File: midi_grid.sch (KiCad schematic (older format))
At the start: 3 parts, among them J1 USB_OTG, J2 3.5mm jack, J3 3.5mm jack

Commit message: multiple schematic and pcb changes
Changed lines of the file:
@@
 F0 "grid" 60
 F1 "grid.sch" 60
-F2 "BUTTON[1..4]" O R 4800 3400 60
-F3 "RED[1..4]" I R 4800 3000 60
-F4 "GREEN[1..4]" I R 4800 3100 60
-F5 "BLUE[1..4]" I R 4800 3200 60
+F2 "GRID_BUTTON[1..4]" O R 4800 3400 60
+F3 "PWM_RED[1..4]" I R 4800 3000 60
+F4 "PWM_GREEN[1..4]" I R 4800 3100 60
+F5 "PWM_BLUE[1..4]" I R 4800 3200 60
 F6 "COLUMN[1..6]" I R 4800 3600 60
 $EndSheet

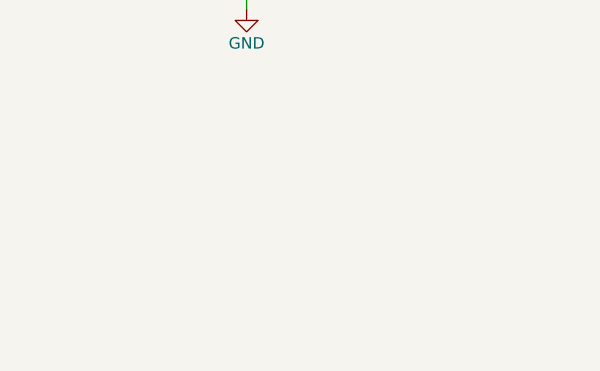
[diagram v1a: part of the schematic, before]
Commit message: added logos to pcb
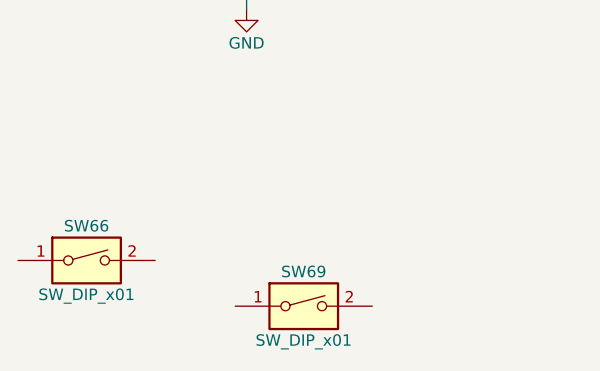
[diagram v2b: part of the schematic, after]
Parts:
- added SW66: SW_DIP_x01, ProjectLib:Logo_OSHW, symbol SW_DIP_x01
- added SW69: SW_DIP_x01, ProjectLib:qr_url, symbol SW_DIP_x01
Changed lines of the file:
@@
 NoConn ~ 2900 4600
 NoConn ~ 2900 4300
+$Comp
+L SW_DIP_x01 SW66
+U 1 1 5A53D346
+P 1800 6500
+F 0 "SW66" H 1800 6650 50  0000 C CNN
+F 1 "SW_DIP_x01" H 1800 6350 50  0000 C CNN
+F 2 "ProjectLib:Logo_OSHW" H 1800 6500 50  0001 C CNN
+F 3 "" H 1800 6500 50  0001 C CNN
+	1    1800 6500
+	1    0    0    -1
+$EndComp
+$Comp
+L SW_DIP_x01 SW69
+U 1 1 5A53DA73
+P 2750 6700
+F 0 "SW69" H 2750 6850 50  0000 C CNN
+F 1 "SW_DIP_x01" H 2750 6550 50  0000 C CNN
+F 2 "ProjectLib:qr_url" H 2750 6700 50  0001 C CNN
+F 3 "" H 2750 6700 50  0001 C CNN
+	1    2750 6700
+	1    0    0    -1
+$EndComp
 $EndSCHEMATC

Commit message: pcb development
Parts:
- GR1: renamed from SW66; value SW_DIP_x01 -> OSHW logo; symbol SW_DIP_x01 -> Graphical
- GR2: renamed from SW69; value SW_DIP_x01 -> QR code; symbol SW_DIP_x01 -> Graphical
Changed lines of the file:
@@
 NoConn ~ 2900 4300
 $Comp
-L SW_DIP_x01 SW66
+L Graphical GR1
 U 1 1 5A53D346
-P 1800 6500
-F 0 "SW66" H 1800 6650 50  0000 C CNN
-F 1 "SW_DIP_x01" H 1800 6350 50  0000 C CNN
-F 2 "ProjectLib:Logo_OSHW" H 1800 6500 50  0001 C CNN
-F 3 "" H 1800 6500 50  0001 C CNN
-	1    1800 6500
+P 10400 6200
+F 0 "GR1" H 10400 6350 50  0000 C CNN
+F 1 "OSHW logo" H 10400 6050 50  0000 C CNN
+F 2 "ProjectLib:Logo_OSHW" H 10400 6200 50  0001 C CNN
+F 3 "" H 10400 6200 50  0001 C CNN
+	1    10400 6200
 	1    0    0    -1
 $EndComp
 $Comp
-L SW_DIP_x01 SW69
+L Graphical GR2
 U 1 1 5A53DA73
-P 2750 6700
-F 0 "SW69" H 2750 6850 50  0000 C CNN
-F 1 "SW_DIP_x01" H 2750 6550 50  0000 C CNN
-F 2 "ProjectLib:qr_url" H 2750 6700 50  0001 C CNN
-F 3 "" H 2750 6700 50  0001 C CNN
-	1    2750 6700
+P 10900 6200
+F 0 "GR2" H 10900 6350 50  0000 C CNN
+F 1 "QR code" H 10900 6050 50  0000 C CNN
+F 2 "ProjectLib:qr_url" H 10900 6200 50  0001 C CNN
+F 3 "" H 10900 6200 50  0001 C CNN
+	1    10900 6200
 	1    0    0    -1
 $EndComp
